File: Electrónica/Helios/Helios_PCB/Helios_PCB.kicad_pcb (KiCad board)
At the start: 2 copper layers, 35 x 30.3 mm, 18 parts, among them J0 Connector J0, J1 Connector J1, Q1 AO3400A, U0 OPA2380, U1 OPA2380

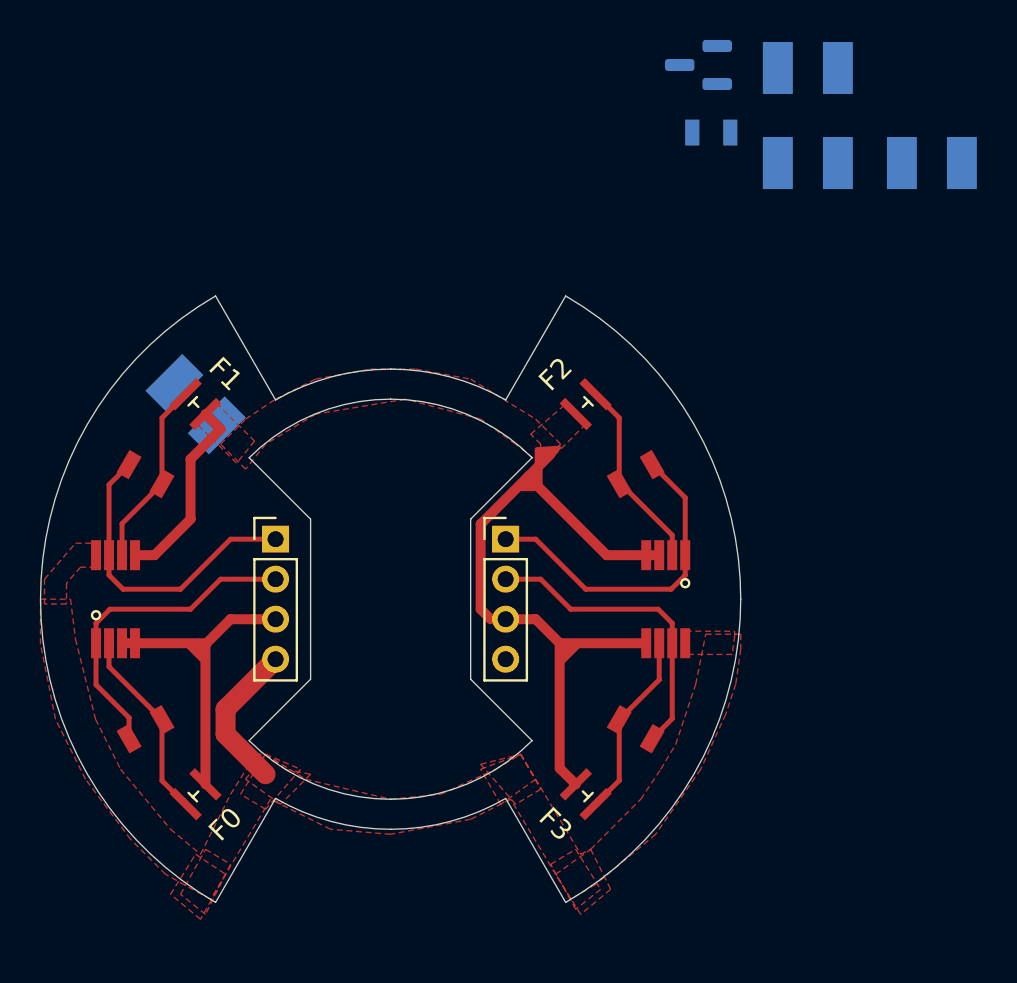
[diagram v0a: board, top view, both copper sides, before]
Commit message: Revert "Revert "Helios: Bot added resistance""
This reverts commit b6ec3ea842d96de8bcfcf6a4a844077dd7699937.
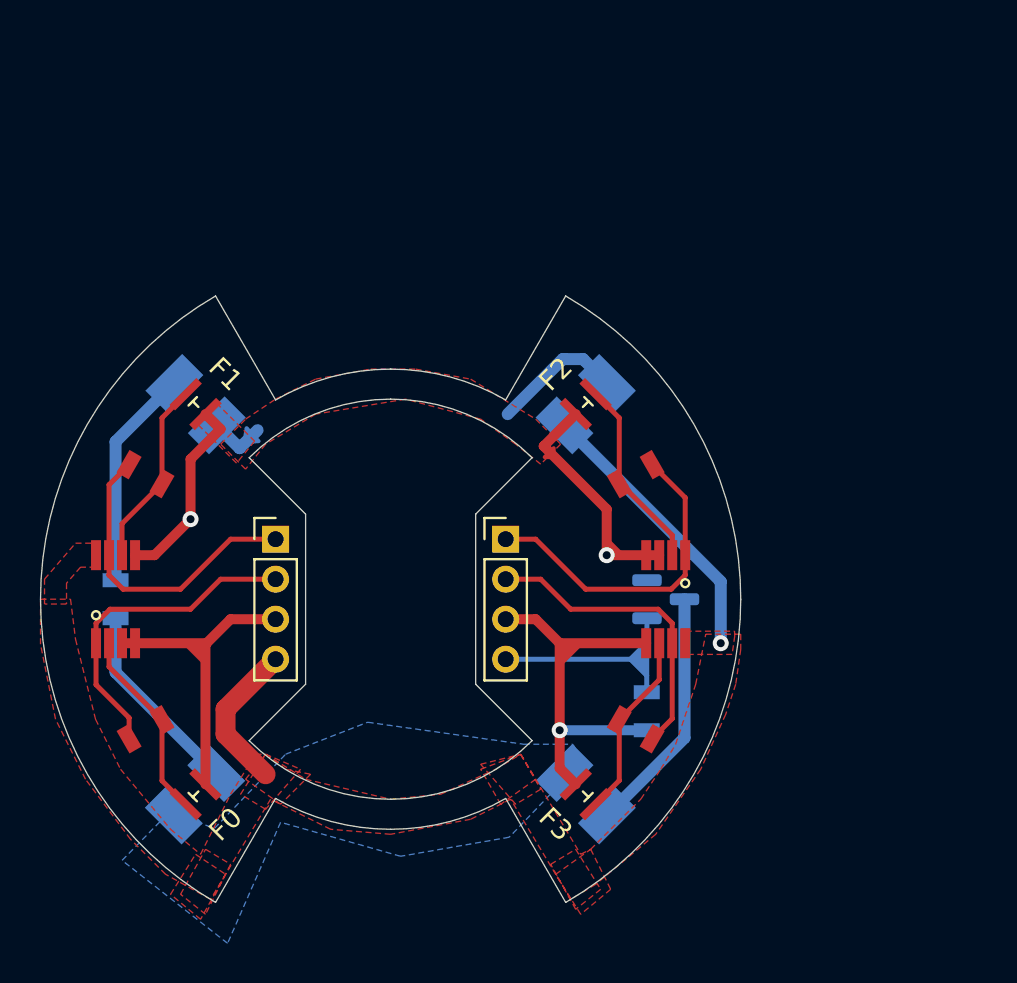
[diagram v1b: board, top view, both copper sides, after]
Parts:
- added R6: R, Helios:RS_0805, B.Cu at (136.2, 100.0)
- moved D0 44.0 mm to (140.2, 109.8), turned to 45 degrees
- moved D3 38.0 mm to (159.8, 109.8), turned to 135 degrees
- moved R5 29.1 mm to (162.8, 105.6), turned to -90 degrees
- moved Q1 26.8 mm to (163.8, 100.0), turned to 0 degrees
- moved D2 21.1 mm to (159.8, 90.2), turned to -135 degrees
- turned D1 to -45 degrees
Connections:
- D0 pad 1: Net-(Q1-Pad3) -> Net-(D0-Pad1)
- D0 pad 2: Net-(D0-Pad2) -> Net-(R6-Pad1)
- D1 pad 1: Net-(D0-Pad2) -> Net-(D1-Pad1)
- D2 pad 2: Net-(D2-Pad2) -> VCC
- D3 pad 1: Net-(D2-Pad2) -> Net-(D3-Pad1)
- D3 pad 2: VCC -> Net-(D0-Pad1)
- Q1 pad 3: Net-(Q1-Pad3) -> Net-(D3-Pad1)
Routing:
- net VCC: track 7.61 -> 21.7 mm, vias 0 -> 1
- net Net-(D3-Pad1): track 0.00 -> 12.4 mm
- net Net-(D1-Pad1): track 0.00 -> 11.1 mm
- net LED: track 0.00 -> 10.6 mm
- net Net-(R6-Pad1): track 0.00 -> 9.83 mm
- net Net-(D1-Pad2): track 0.00 -> 9.48 mm
- net GND: track 60.4 -> 57.6 mm, vias 0 -> 3
- added copper zone on B.Cu, net Net-(D0-Pad1)
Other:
- outline, holes or cut-outs redrawn

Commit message: Revert "Helios: Bot added resistance"
This reverts commit d0f403256e0d7f179b5c0dd237f6584baac4939d.
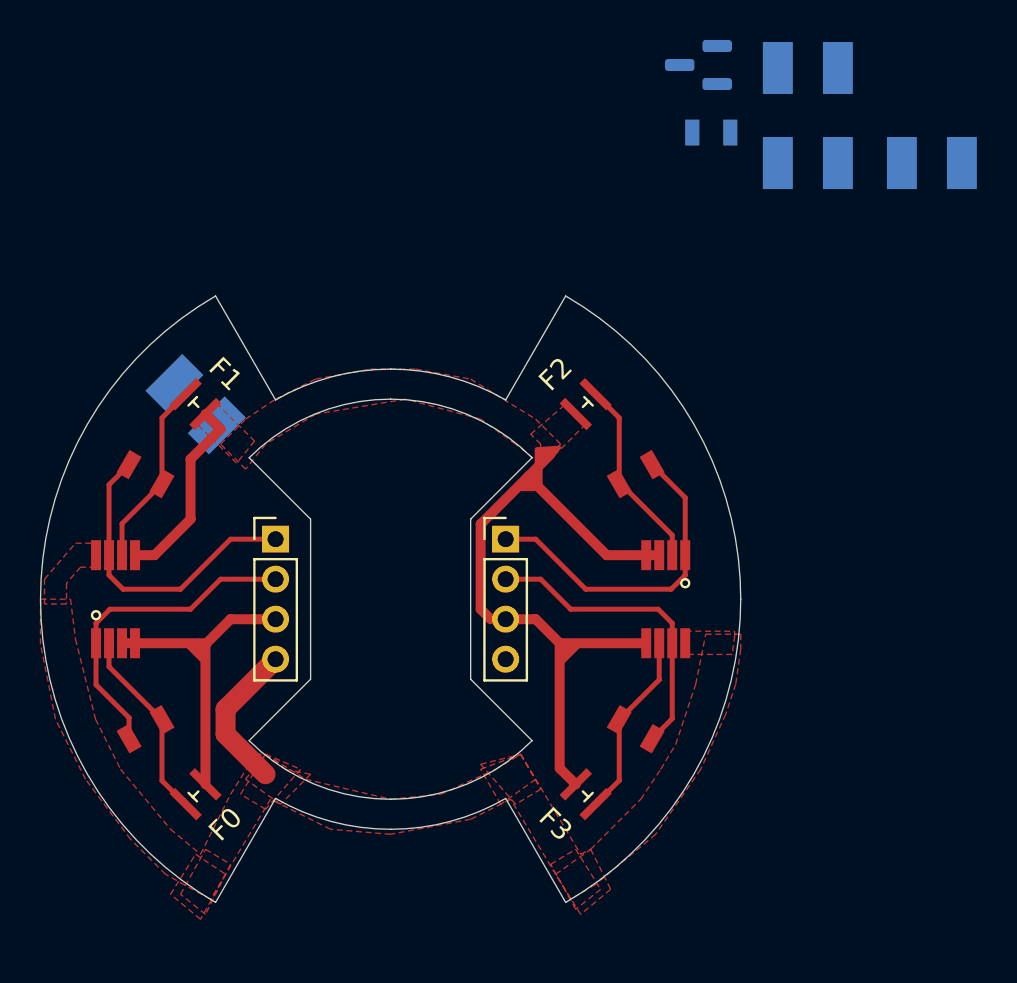
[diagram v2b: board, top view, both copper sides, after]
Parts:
- removed R6: R, Helios:RS_0805
- moved D0 44.0 mm to (170.9, 78.2), turned to 180 degrees
- moved D3 38.0 mm to (170.9, 73.5), turned to 180 degrees
- moved R5 29.1 mm to (166.0, 76.7), turned to 180 degrees
- moved Q1 26.8 mm to (165.4, 73.3), turned to 180 degrees
- moved D2 21.1 mm to (177.1, 78.2), turned to 180 degrees
- turned D1 to 135 degrees
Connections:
- D0 pad 1: Net-(D0-Pad1) -> Net-(Q1-Pad3)
- D0 pad 2: Net-(R6-Pad1) -> Net-(D0-Pad2)
- D1 pad 1: Net-(D1-Pad1) -> Net-(D0-Pad2)
- D2 pad 2: VCC -> Net-(D2-Pad2)
- D3 pad 1: Net-(D3-Pad1) -> Net-(D2-Pad2)
- D3 pad 2: Net-(D0-Pad1) -> VCC
- Q1 pad 3: Net-(D3-Pad1) -> Net-(Q1-Pad3)
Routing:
- net VCC: track 21.7 -> 7.61 mm, vias 1 -> 0
- net Net-(D3-Pad1): track 12.4 -> 0.00 mm
- net Net-(D1-Pad1): track 11.1 -> 0.00 mm
- net LED: track 10.6 -> 0.00 mm
- net Net-(R6-Pad1): track 9.83 -> 0.00 mm
- net Net-(D1-Pad2): track 9.48 -> 0.00 mm
- net GND: track 57.6 -> 60.4 mm, vias 3 -> 0
- removed copper zone on B.Cu, net Net-(D0-Pad1)
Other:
- outline, holes or cut-outs redrawn
